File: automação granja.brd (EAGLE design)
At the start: 160 x 100 mm, 70 parts, among them IC1 MEGA8-P, IC10 A1322UA, IC11 A1322UA, IC12 A1322UA, IC2 MAX481CPA, IC3 A1322UA, IC4 A1322UA, IC7 A1322UA, IC8 A1322UA, IC9 A1322UA, K1 G2RA, K2 G2RA, K3 G2RA, K4 G2RA, K5 G2RA, K6 G2RA, K7 G2RA, K8 G2RA, Q1 BC548B, Q2 BC548B, Q3 BC548B, Q4 BC548B, Q6 BC548B, Q7 BC548B, Q8 BC548B, Q9 BC548B

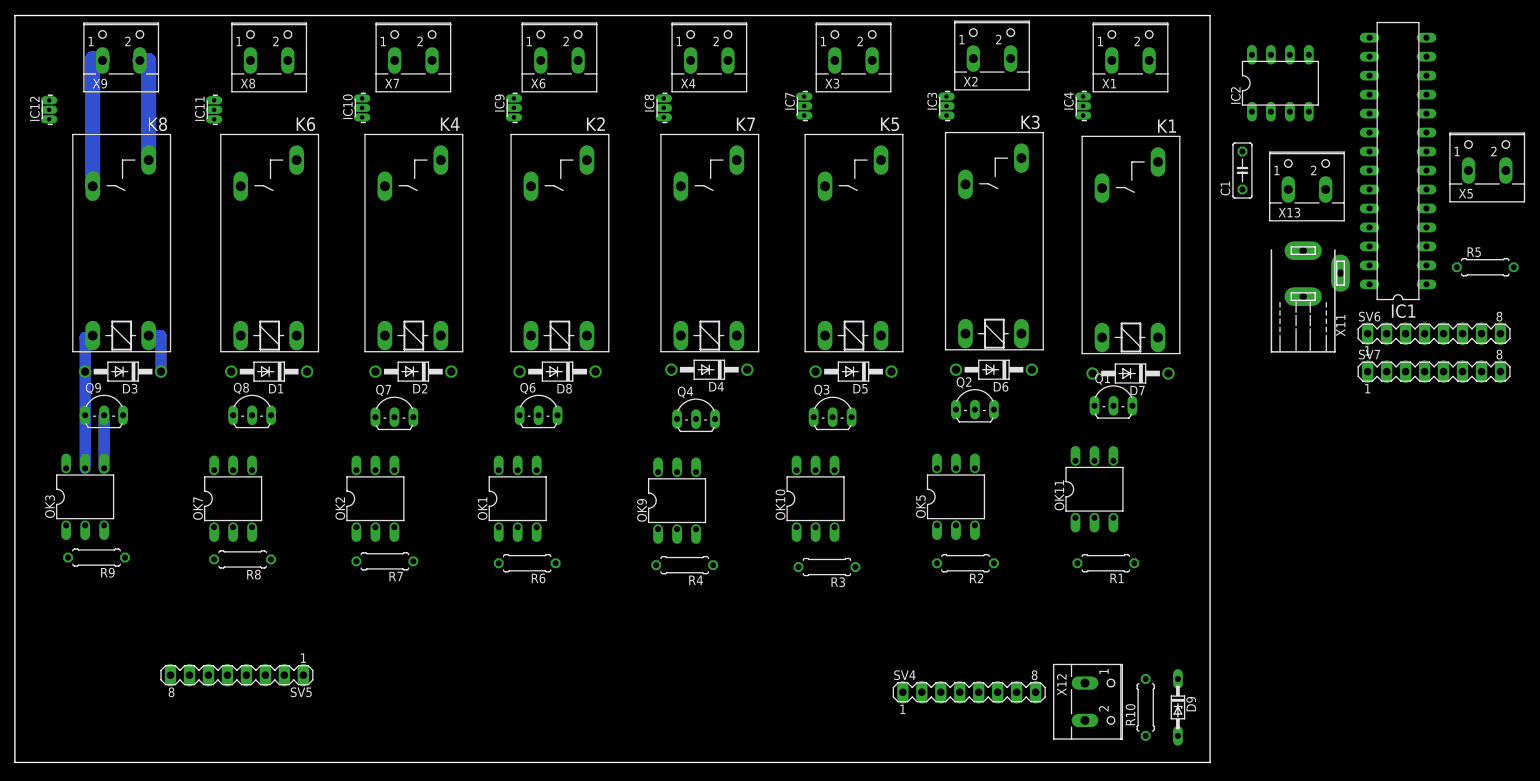
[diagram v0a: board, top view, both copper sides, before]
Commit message: separadas controle de atuação e realimentação
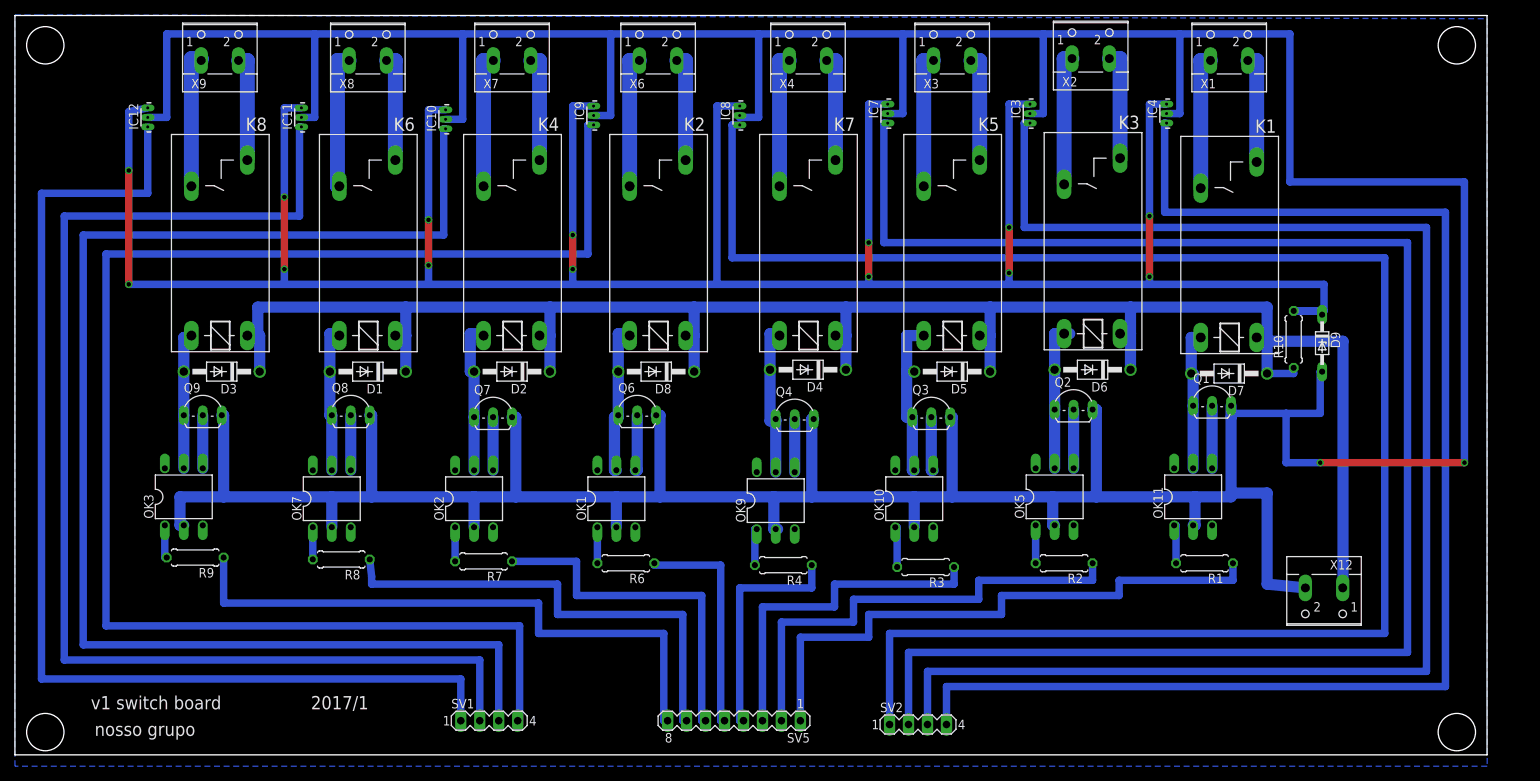
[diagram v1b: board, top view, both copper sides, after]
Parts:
- removed C1: (no value), rcl:C050-025X075
- removed IC1: MEGA8-P, atmel:DIL28-3
- removed IC2: MAX481CPA, maxim:DIL08
- removed R5: (no value), rcl:0207/7
- removed SV4, SV6, SV7: (no value), con-lstb:MA08-1
- removed X11: (no value), con-conrad:733980-62
- removed X13, X5: (no value), con-wago-500:W237-102
- added SV1, SV2: (no value), con-lstb:MA04-1
- moved SV5 66.8 mm to (96.3, 5.59)
- moved R10 53.1 mm to (171.2, 56.6)
- moved D9 52.4 mm to (175.0, 56.1)
- moved X12 33.8 mm to (175.3, 22.1), turned to 180 degrees
- moved IC12 13.2 mm to (17.8, 86.4)
- moved OK11 13.2 mm to (157.7, 35.6)
- moved OK5 13.2 mm to (139.2, 35.6)
- moved OK2 13.2 mm to (61.5, 35.3)
- moved OK3 13.2 mm to (22.6, 35.6)
- moved R8 13.2 mm to (43.7, 27.2)
- moved D3 13.2 mm to (27.7, 52.3)
- moved Q9 13.2 mm to (25.1, 47.8)
- moved D1 13.2 mm to (47.2, 52.3)
- moved D2 13.2 mm to (66.5, 52.3)
- moved D4 13.2 mm to (106.2, 52.6)
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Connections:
- removed net 12VCTRL: C1.2, X11.2, X13.2
- removed net GND: C1.1, IC1.21, IC1.8, IC2.5, X11.1, X11.3, X13.1
- removed net N$13: IC2.7, R5.2, X5.2
- removed net N$35: IC2.6, R5.1, X5.1
- removed net N$41: IC2.8
- removed net N$42: IC1.7
- removed net N$43: IC1.10
- removed net N$45: IC1.20
- removed net N$46: IC1.22
- removed net N$47: IC1.1
- removed net N$48: IC1.23
- removed net N$49: IC1.24
- removed net N$50: IC1.25
- removed net N$51: IC1.26
- removed net N$52: IC1.27
- removed net N$53: IC1.28
- removed net N$54: IC1.2
- removed net N$55: IC1.3, IC2.4
- removed net N$56: IC1.4, IC2.2, IC2.3
- removed net N$57: IC1.5
- removed net N$58: IC1.6
- removed net N$59: IC1.11
- removed net N$60: IC1.12
- removed net N$61: IC1.13
- removed net N$62: IC1.14
- removed net N$63: IC1.15
- removed net N$64: IC1.16
- removed net N$65: IC1.17
- removed net N$66: IC1.18
- removed net N$67: IC1.19
- removed net N$84: D9.A, IC10.2, IC11.2, IC12.2, IC3.2, IC4.2, IC7.2, IC8.2, IC9.2
- net GNDSW: now also D9.A, IC10.2, IC11.2, IC12.2, IC3.2, IC4.2, IC7.2, IC8.2, IC9.2
- net OP1: now also SV1.1; no longer SV4.1
- net OP2: now also SV1.2; no longer SV4.2
- net OP3: now also SV1.3; no longer SV4.3
- net OP4: now also SV1.4; no longer SV4.4
- net OP5: now also SV2.1; no longer SV4.5
- net OP6: now also SV2.2; no longer SV4.6
- net OP7: now also SV2.3; no longer SV4.7
- net OP8: now also SV2.4; no longer SV4.8
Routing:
- net GNDSW: track 0.00 -> 672.4 mm, vias 0 -> 2
- net N$24: track 0.00 -> 382.8 mm, vias 0 -> 14
- net 12V: track 6.48 -> 262.7 mm
- net OP5: track 0.00 -> 235.0 mm
- net OP6: track 0.00 -> 217.9 mm
- net OP7: track 0.00 -> 201.9 mm
- net OP4: track 0.00 -> 200.9 mm
- net OP8: track 0.00 -> 185.2 mm
- net OP3: track 0.00 -> 183.4 mm
- net OP2: track 0.00 -> 166.9 mm
- net OP1: track 0.00 -> 149.9 mm
- net S8: track 0.00 -> 81.3 mm
- net S1: track 0.00 -> 79.0 mm
- net S7: track 0.00 -> 63.8 mm
- net S2: track 0.00 -> 62.7 mm
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- added copper zone on layer 16, net GNDSW
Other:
- board size 160 x 100 mm -> 197.1 x 99 mm
- board text added: "2017/1"
- board text added: "nosso grupo"
- board text added: "v1 switch board"
